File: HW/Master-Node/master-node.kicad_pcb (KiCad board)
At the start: 2 copper layers, 100 x 60 mm, 84 parts, among them J1 CONN_01X04, J2 CONN_01X06, J3 USB_OTG, J4 CONN_01X04, J5 CONN_01X08, J6 CONN_01X04, M1 NRF24L01, Q2 C1815, SW1 SW_Push, U1 ASM1117, U2 MC34063, U3 MAX485, U4 STM32F103C8, U5 ESP-12, Y1 Crystal, Y2 Crystal_GND3

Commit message: upload layout
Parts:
- added C29: 100nF, Capacitors_SMD:C_0805_HandSoldering, F.Cu at (155.7, 72.8)
- added R32: 10k, Resistors_SMD:R_0805_HandSoldering, F.Cu at (155.7, 78.9)
- added SW2: SW_Push, nhantt-kicad-lib:Button-6mm-smd, F.Cu at (160.5, 76.0)
- moved J5 78.5 mm to (150.9, 73.1), turned to 270 degrees
- moved C19 64.9 mm to (149.8, 83.4), turned to 180 degrees
- moved J6 61.5 mm to (151.1, 80.3), turned to 270 degrees
- moved R19 60.9 mm to (143.4, 84.9), turned to 270 degrees
- moved R20 57.7 mm to (145.9, 84.9), turned to 270 degrees
- moved U1 41.3 mm to (113.0, 92.5), turned to 180 degrees
- moved C4 40.1 mm to (124.0, 92.0)
- moved C5 39.4 mm to (120.5, 92.4)
- moved J3 31.0 mm to (94.4, 118.1)
- moved C20 29.9 mm to (131.0, 120.5), turned to 90 degrees
- moved R17 28.4 mm to (101.7, 121.8), turned to 180 degrees
- moved R14 27.5 mm to (101.7, 124.4), turned to 180 degrees
- moved D2 27.1 mm to (122.0, 73.0)
- moved R26 26.9 mm to (134.2, 120.8)
- moved R27 26.8 mm to (137.3, 120.8)
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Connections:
- J1 pad 2: /A -> /B
- J1 pad 3: /B -> /A
- R15 pad 1: /485TX -> /485_TX
- U4 pad 21: /485_TX -> /ESP_RX
- U4 pad 22: /485_RX -> /ESP_TX
- U4 pad 30: /ESP_RX -> /485_TX
- U4 pad 31: /ESP_TX -> /485_RX
- U4 pad 38: Net-(U4-Pad38) -> /CFG_nRF
- U4 pad 42: /I2C_SCL -> /SCL
- U4 pad 43: /I2C_SDA -> /SDA
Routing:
- net GND: track 0.00 -> 396.7 mm, vias 0 -> 9
- net +3V3: track 0.00 -> 139.1 mm, vias 0 -> 1
- net +5V: track 0.00 -> 118.6 mm, vias 0 -> 7
- net /ESP_RST: track 0.00 -> 53.1 mm, vias 0 -> 2
- net /SMART_CFG: track 0.00 -> 48.4 mm, vias 0 -> 4
- net /ESP_EN: track 0.00 -> 44.9 mm, vias 0 -> 2
- net /ESP_RX: track 0.00 -> 34.9 mm, vias 0 -> 2
- net /ESP_TX: track 0.00 -> 34.2 mm, vias 0 -> 2
- net /nRF_IRQ: track 0.00 -> 32.9 mm
- net /ESP_PRO: track 0.00 -> 32.7 mm, vias 0 -> 2
- net Net-(BT1-Pad1): track 0.00 -> 32.0 mm, vias 0 -> 4
- net /nRF_CE: track 0.00 -> 29.1 mm, vias 0 -> 1
- net /nRF_MISO: track 0.00 -> 28.8 mm, vias 0 -> 1
- net /I/O1: track 0.00 -> 27.3 mm
- net /USB_DIS: track 0.00 -> 27.0 mm
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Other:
- board size 100 x 60 mm -> 85 x 60 mm
- net class Default: trace_width 0.25 -> 0.254; via_dia 0.6 -> 1.1; via_drill 0.4 -> 0.6

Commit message: complete layout master node
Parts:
- added REF**: Vit-4mm, nhantt-kicad-lib:Vit-4mm, F.Cu at (93.0, 127.0)
- added REF**: Vit-4mm, nhantt-kicad-lib:Vit-4mm, F.Cu at (177.0, 127.0)
- added REF**: Vit-4mm, nhantt-kicad-lib:Vit-4mm, F.Cu at (94.0, 74.0)
- added REF**: Vit-4mm, nhantt-kicad-lib:Vit-4mm, F.Cu at (177.0, 74.0)
- moved J3 1.14 mm to (94.5, 117.0)
- moved C22 1.06 mm to (128.2, 104.6)
- moved C23 0.98 mm to (125.6, 104.3)
- moved C16 0.27 mm to (132.5, 94.0)
- moved C7 0.16 mm to (132.1, 81.4)
- turned J1 to 270 degrees
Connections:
- J1 pad 1: GND -> VIN
- J1 pad 2: /B -> /A
- J1 pad 3: /A -> /B
- J1 pad 4: VIN -> GND
- U4 pad 2: Net-(U4-Pad2) -> /USB_DIS
- U4 pad 26: /SCK -> /CLK
- U4 pad 29: /USB_DIS -> Net-(U4-Pad29)
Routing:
- net GND: track 396.7 -> 613.5 mm, vias 9 -> 110
- net +3V3: track 139.1 -> 245.7 mm, vias 1 -> 23
- net /BL: track 0.00 -> 47.8 mm, vias 0 -> 1
- net /CFG_nRF: track 14.2 -> 61.6 mm, vias 0 -> 2
- net /SDA: track 3.25 -> 40.5 mm, vias 0 -> 2
- net /DC: track 0.00 -> 36.6 mm, vias 0 -> 1
- net /RST: track 0.00 -> 36.3 mm, vias 0 -> 1
- net /SCL: track 3.26 -> 34.0 mm, vias 0 -> 2
- net /CE: track 0.00 -> 27.9 mm, vias 0 -> 2
- net /CLK: track 0.00 -> 26.4 mm
- net /485_RX: track 2.72 -> 28.7 mm, vias 0 -> 3
- net /DIN: track 0.00 -> 26.0 mm
- net /USBDM: track 19.9 -> 45.7 mm, vias 0 -> 2
- net /USBDP: track 23.5 -> 46.5 mm, vias 0 -> 2
- net /485_TX: track 0.00 -> 22.8 mm, vias 0 -> 3
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- added copper zone on F.Cu, net +12V
- added copper zone on B.Cu, net +3V3
- added copper zone on F.Cu, net +3V3
- added copper zone on B.Cu, net +5V
- added copper zone on F.Cu, net +5V
- added copper zone on B.Cu, net GND
- added copper zone on F.Cu, net GND
- added copper zone on F.Cu, net Net-(BT1-Pad1)
- added copper zone on F.Cu, net Net-(D3-Pad1)
- added copper zone on F.Cu, net Net-(Q2-Pad3)
- added copper zone on F.Cu, net Net-(R1-Pad2)
- added copper zone on F.Cu, net VIN
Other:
- board size 85 x 60 mm -> 90 x 60 mm

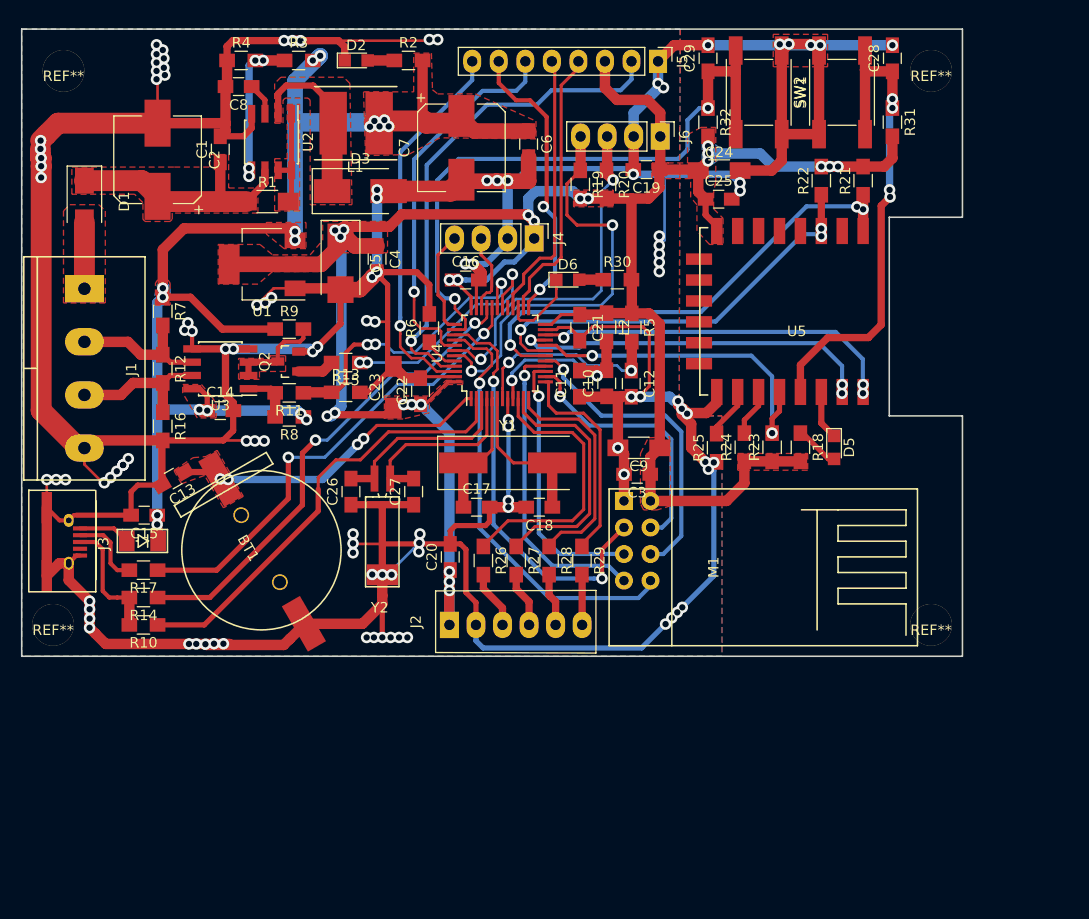
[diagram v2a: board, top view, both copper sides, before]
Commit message: modified label
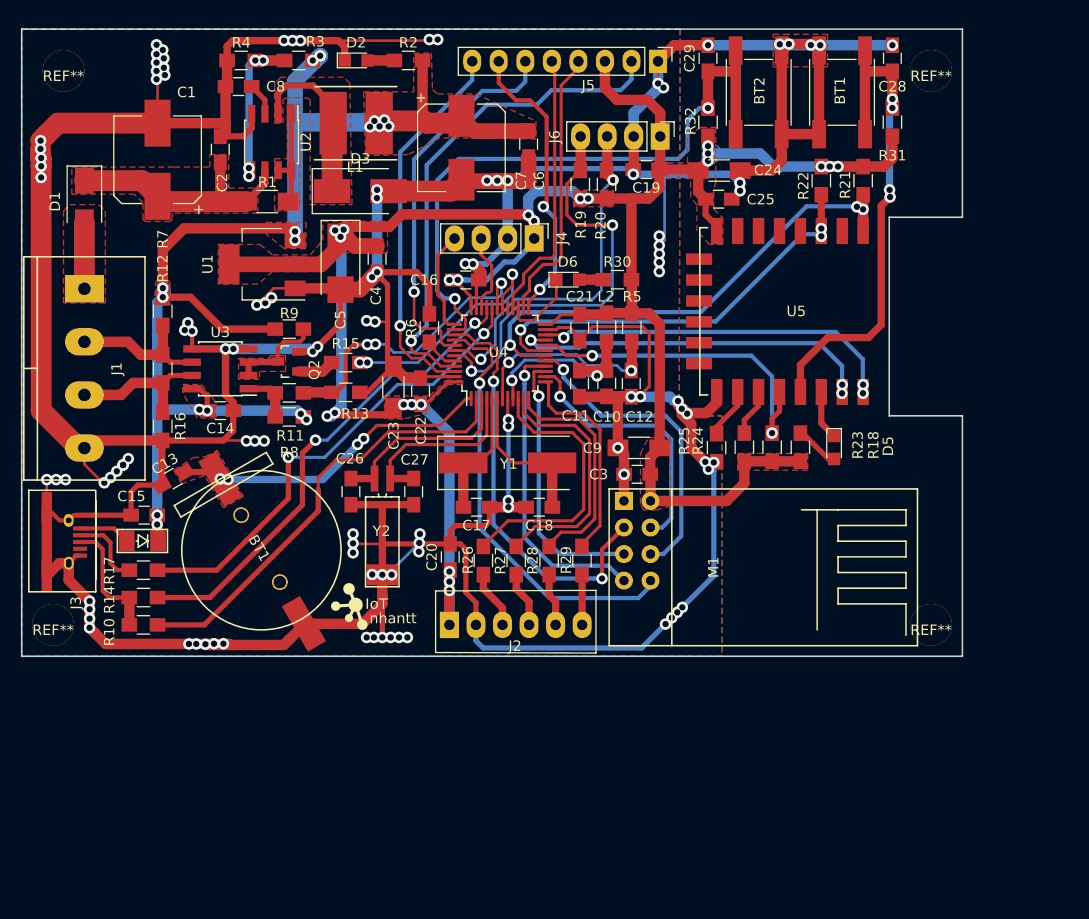
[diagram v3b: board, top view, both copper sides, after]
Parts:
- added ?: , nhantt-kicad-lib:logo2, F.Cu at (122.0, 125.1)
- renumbered SW1 to BT1, SW2 to BT2
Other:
- board text added: "nhantt"
